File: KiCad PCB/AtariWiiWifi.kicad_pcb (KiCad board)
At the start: 2 copper layers, 53.3 x 57.1 mm, 18 parts, among them J1A1 Conn_01x09, J2A1 Conn_01x09, U1 PCAL6416APW, U2 AD5242, U3 AD5242, U4 ESP32

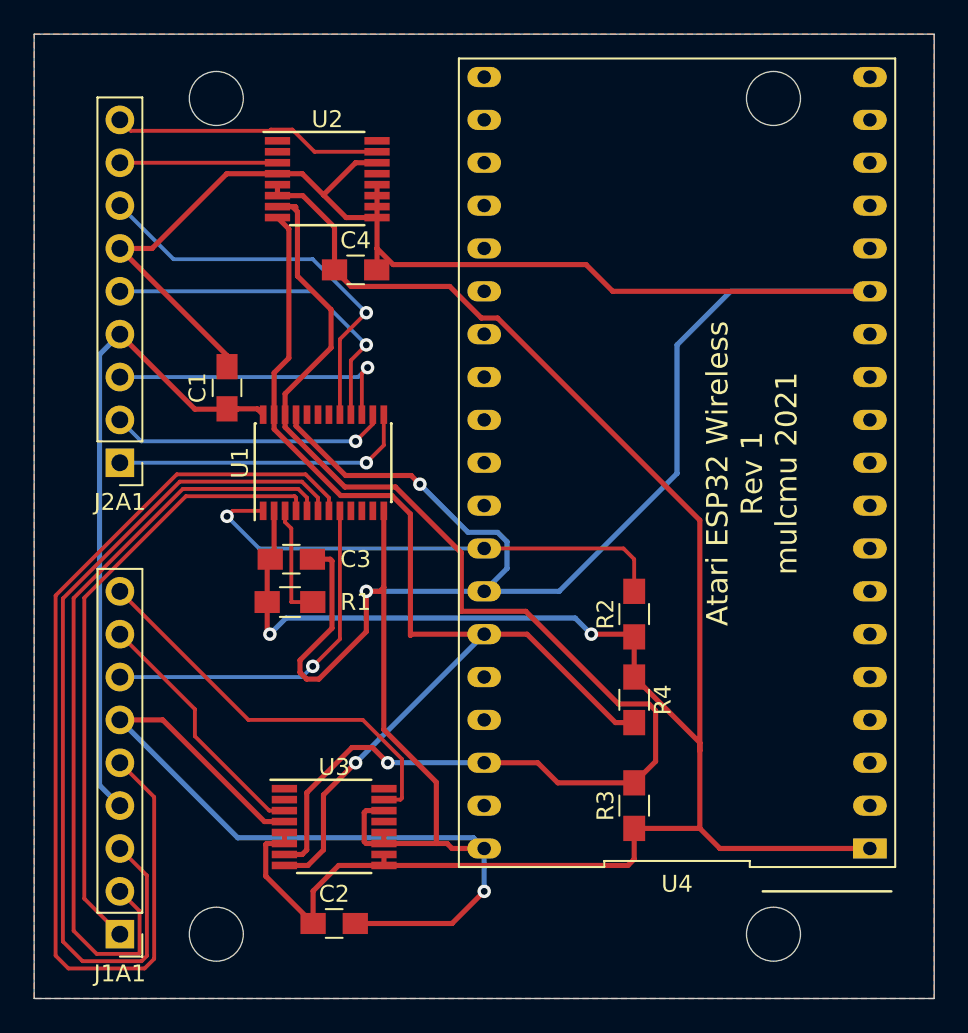
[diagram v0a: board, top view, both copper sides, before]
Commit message: Update PCB to Rev 2
Fixed Digital pots connected to ground instead of +5.

Added jumper to power ESP from Atari
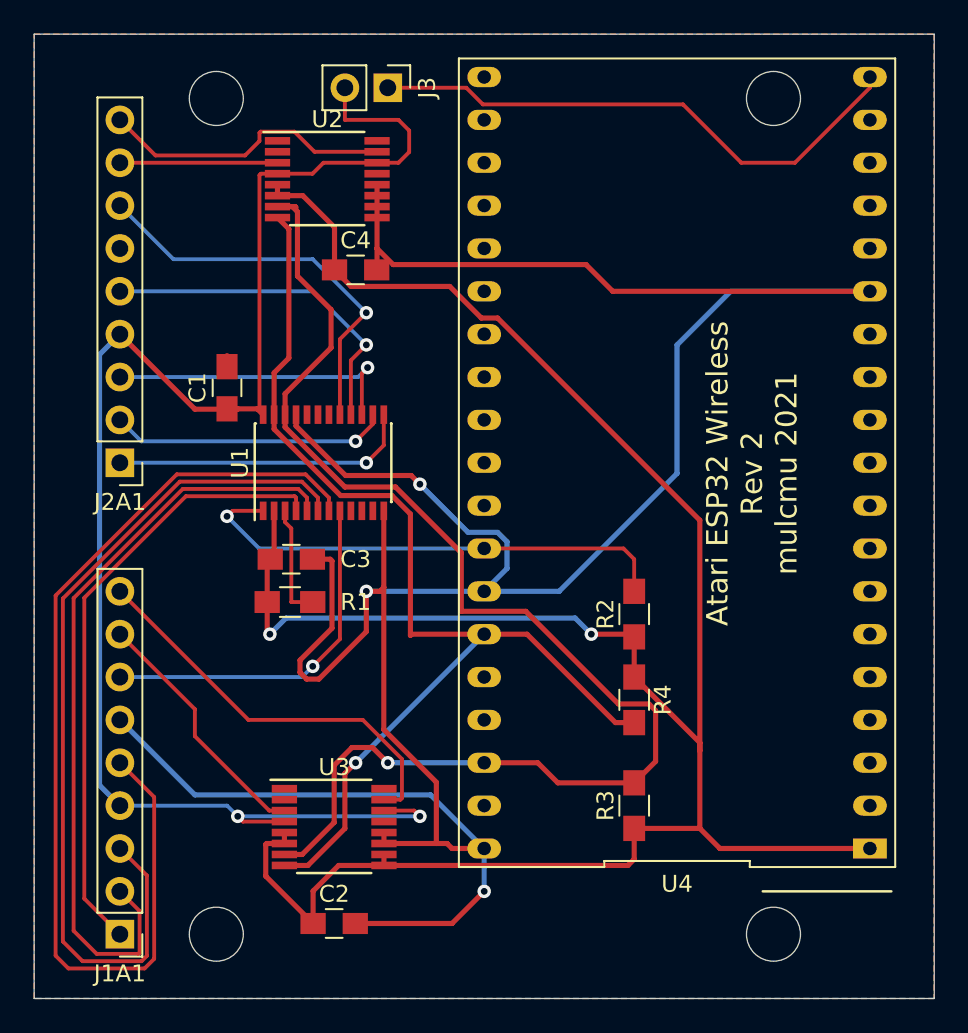
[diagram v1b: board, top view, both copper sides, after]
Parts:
- added J3: Conn_01x02_Male, Pin_Headers:Pin_Header_Straight_1x02_Pitch2.54mm, F.Cu at (145.4, 70.5)
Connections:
- C1 pad 1: /J1_5V -> +5V
- J1A1 pad 4: /J1_5V -> +5V
- J2A1 pad 4: /J1_5V -> +5V
- U1 pad 24: /J1_5V -> +5V
- U2 pad 14: GND -> +5V
- U2 pad 4: GND -> +5V
- U3 pad 14: GND -> +5V
- U3 pad 4: GND -> +5V
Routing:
- net +5V: track 0.00 -> 93.6 mm, vias 0 -> 2
- net GND: track 225.5 -> 178.0 mm
- net /J1_5V: track 39.4 -> 0.00 mm
- net Net-(J3-Pad1): track 0.00 -> 32.9 mm
- net /J2_PotB: track 16.1 -> 17.5 mm
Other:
- board text added: "Atari ESP32 Wireless Rev 2 mulcmu 2021"
- board text removed: "Atari ESP32 Wireless Rev 1 mulcmu 2021"

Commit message: Rev 3 PCB
Update Rev 3 PCB files.
Small Tweak to Schematic for extra bypass cap.
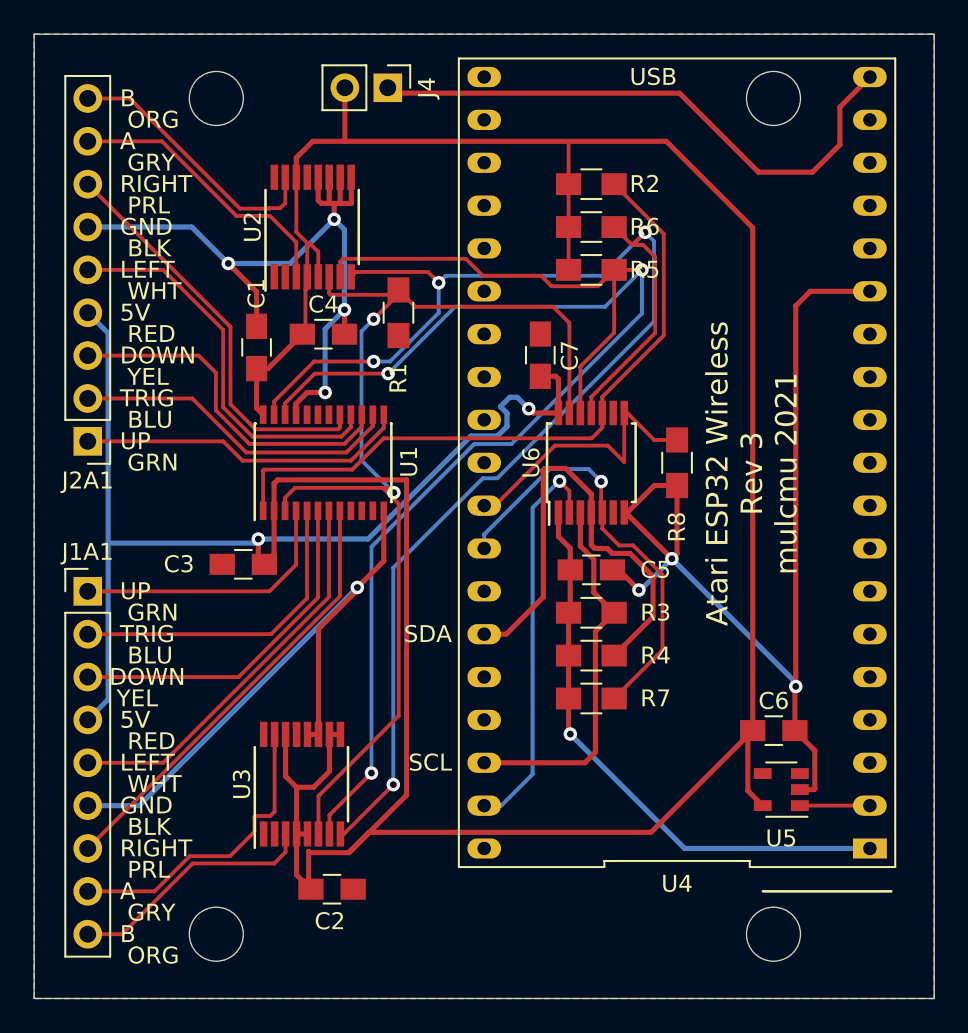
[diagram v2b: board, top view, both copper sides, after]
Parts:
- removed J3: Conn_01x02_Male, Pin_Headers:Pin_Header_Straight_1x02_Pitch2.54mm
- added C5: C, Capacitors_SMD:C_0805_HandSoldering, F.Cu at (157.5, 99.1)
- added C6: C, Capacitors_SMD:C_0805_HandSoldering, F.Cu at (168.3, 108.6)
- added C7: C, Capacitors_SMD:C_0805_HandSoldering, F.Cu at (154.5, 86.3)
- added J4: Conn_01x02_Male, Pin_Headers:Pin_Header_Straight_1x02_Pitch2.54mm, F.Cu at (145.4, 70.5)
- added R5: R, Resistors_SMD:R_0805_HandSoldering, F.Cu at (157.5, 78.7)
- added R6: R, Resistors_SMD:R_0805_HandSoldering, F.Cu at (157.5, 81.3)
- added R7: R, Resistors_SMD:R_0805_HandSoldering, F.Cu at (157.5, 106.7)
- added R8: R, Resistors_SMD:R_0805_HandSoldering, F.Cu at (162.6, 92.7)
- added U5: MIC2775, TO_SOT_Packages_SMD:SOT-23-5, F.Cu at (168.7, 112.1)
- added U6: TXS0104E, Housings_SSOP:TSSOP-14_4.4x5mm_Pitch0.65mm, F.Cu at (157.5, 92.7)
- moved R2 25.6 mm to (157.5, 76.2), turned to 0 degrees
- moved J1A1 20.4 mm to (127.6, 100.3), turned to 0 degrees
- moved R1 18.3 mm to (146.1, 83.8), turned to 270 degrees
- moved R3 11.7 mm to (157.5, 101.6), turned to 0 degrees
- moved C4 4.26 mm to (141.6, 85.1)
- moved R4 3.65 mm to (157.5, 104.1), turned to 0 degrees
- moved U3 3.17 mm to (140.3, 111.8), turned to 90 degrees
- moved U2 2.96 mm to (141.0, 78.7), turned to 90 degrees
- moved C1 2.96 mm to (137.6, 85.9)
- moved C3 2.86 mm to (136.9, 98.7), turned to 180 degrees
- moved J2A1 2.29 mm to (127.6, 91.4)
- moved C2 2.04 mm to (142.1, 118.0)
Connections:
- net Net-(U1-Pad10) renamed /J3_TRIG
- net Net-(U1-Pad11) renamed /J3_DOWN
- net Net-(U1-Pad18) renamed /J3_LEFT
- net Net-(U1-Pad19) renamed /J3_RIGHT
- net Net-(U1-Pad9) renamed /J3_UP
- C2 pad 1: +3V3 -> +5V
- C3 pad 1: +3V3 -> +5V
- C4 pad 1: +3V3 -> +5V
- R1 pad 1: +3V3 -> /READY
- R1 pad 2: Net-(R1-Pad2) -> GND
- R2 pad 1: +3V3 -> +5V
- R2 pad 2: Net-(R2-Pad2) -> /INT_5
- U1 pad 1: Net-(R2-Pad2) -> /INT_5
- U1 pad 2: +3V3 -> +5V
- U1 pad 22: /SCL -> /SLC_5
- U1 pad 23: /SDA -> /SDA_5
- U1 pad 3: Net-(R1-Pad2) -> /READY
- U2 pad 5: +3V3 -> +5V
- U2 pad 6: +3V3 -> /READY
- U2 pad 7: /SCL -> /SLC_5
- U2 pad 8: /SDA -> /SDA_5
- U3 pad 10: +3V3 -> +5V
- U3 pad 15: /J1_PotB -> /J1_PotA
- U3 pad 3: /J1_PotA -> /J1_PotB
- U3 pad 5: +3V3 -> +5V
- U3 pad 6: +3V3 -> /READY
- U3 pad 7: /SCL -> /SLC_5
- U3 pad 8: /SDA -> /SDA_5
- U3 pad 9: +3V3 -> +5V
- U4 pad 31: Net-(R2-Pad2) -> /INT
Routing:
- net +5V: track 93.6 -> 262.5 mm
- net +3V3: track 138.0 -> 34.6 mm, vias 2 -> 1
- net /SLC_5: track 0.00 -> 96.7 mm, vias 0 -> 3
- net /SDA_5: track 0.00 -> 93.4 mm, vias 0 -> 4
- net /READY: track 0.00 -> 65.7 mm, vias 0 -> 2
- net /SCL: track 78.2 -> 22.5 mm, vias 1 -> 0
- net /INT_5: track 0.00 -> 40.7 mm
- net /J1_LEFT: track 60.7 -> 23.5 mm
- net /SDA: track 65.4 -> 28.6 mm, vias 1 -> 0
- net GND: track 178.0 -> 144.4 mm, vias 3 -> 8
- net /J1_DOWN: track 52.1 -> 20.7 mm
- net Net-(R2-Pad2): track 29.4 -> 0.00 mm, vias 1 -> 0
- net /J1_TRIG: track 45.9 -> 19.1 mm
- net /INT: track 0.00 -> 25.7 mm, vias 0 -> 1
- net Net-(U4-Pad37): track 0.00 -> 23.8 mm, vias 0 -> 1
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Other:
- board text added: "5V"
- board text added: "A"
- board text added: "Atari ESP32 Wireless Rev 3 mulcmu 2021"
- board text added: "B"
- board text added: "BLK"
- board text added: "BLU"
- board text added: "DOWN"
- board text added: "GND"
- board text added: "GRN"
- board text added: "GRY"
- board text added: "LEFT"
- board text added: "ORG"
- board text added: "PRL"
- board text added: "RED"
- board text added: "RIGHT"
- board text added: "SCL"
- board text added: "SDA"
- board text added: "TRIG"
- board text added: "UP"
- board text added: "USB"
- board text added: "WHT"
- board text added: "YEL"
- board text removed: "Atari ESP32 Wireless Rev 2 mulcmu 2021"
